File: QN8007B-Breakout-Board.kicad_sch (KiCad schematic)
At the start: 22 parts, among them J1 U.FL, J2 Conn_01x12, U1 QN8007B, Y1 26 MHz

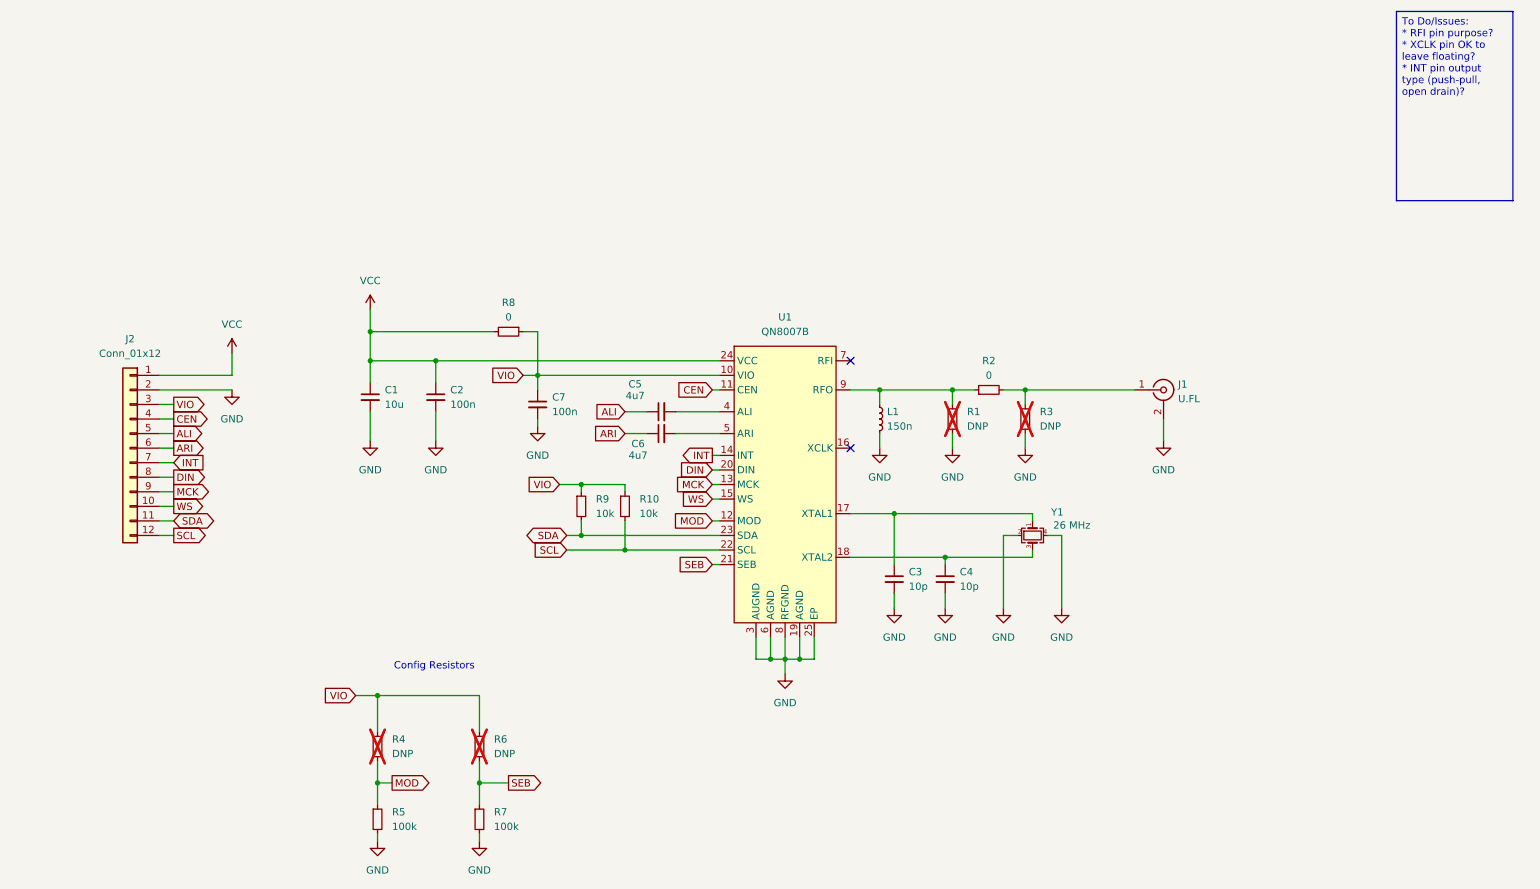
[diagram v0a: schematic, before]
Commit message: Finish routing, small schematic changes to ease routing.
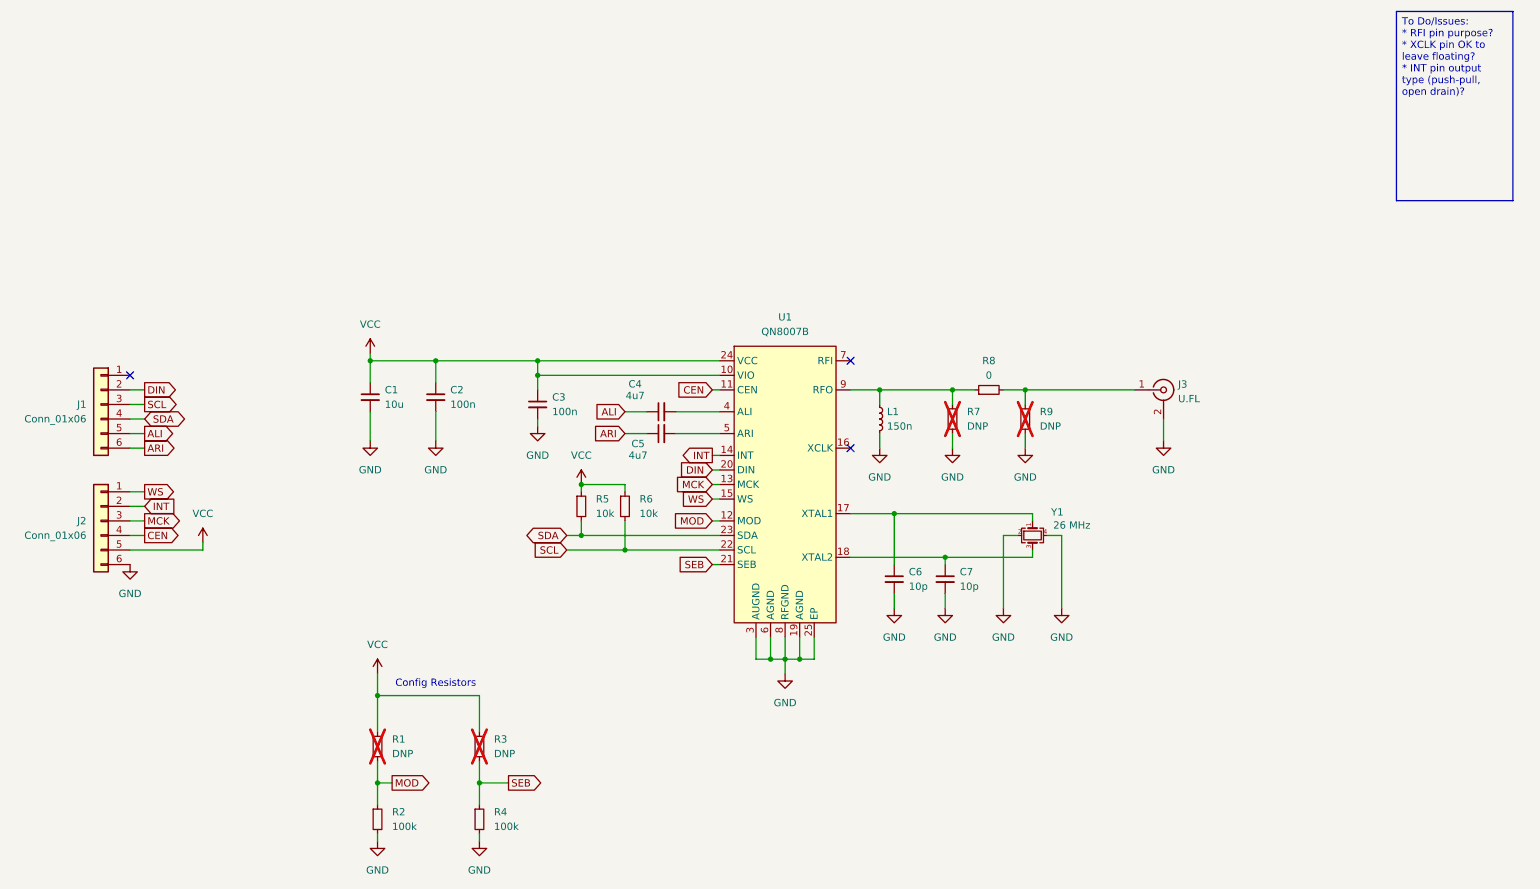
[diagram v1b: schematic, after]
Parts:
- removed J2: Conn_01x12, Connector_PinHeader_2.54mm:PinHeader_1x12_P2.54mm_Vertical, symbol Connector_Generic:Conn_01x12
- removed R8: 0, Resistor_SMD:R_0402_1005Metric, symbol Device:R_Small
- added J1, J2: Conn_01x06, Connector_PinSocket_2.54mm:PinSocket_1x06_P2.54mm_Vertical, symbol Connector_Generic:Conn_01x06
- U1: footprint Package_DFN_QFN:QFN-24-1EP_4x4mm_P0.5mm_EP2.7x2.7mm_ThermalVias -> Package_DFN_QFN:QFN-24-1EP_4x4mm_P0.5mm_EP2.7x2.7mm
- renumbered C7 to C3, C5 to C4, C6 to C5, C3 to C6, C4 to C7, J1 to J3, R4 to R1, R5 to R2, R6 to R3, R7 to R4, R9 to R5, R10 to R6, R1 to R7, R2 to R8, R3 to R9
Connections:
- net VIO is gone; now on net VCC: C3.1, R1.1, R3.1, R5.1, R6.1, U1.10 (VIO)
- net ALI: now also J1.5 (Pin_5)
- net ARI: now also J1.6 (Pin_6)
- net CEN: now also J2.4 (Pin_4)
- net DIN: now also J1.2 (Pin_2)
- net GND: now also J2.6 (Pin_6)
- net INT: now also J2.2 (Pin_2)
- net MCK: now also J2.3 (Pin_3)
- net SCL: now also J1.3 (Pin_3)
- net SDA: now also J1.4 (Pin_4)
- net VCC: now also J2.5 (Pin_5)
- net WS: now also J2.1 (Pin_1)
- no-connect marks 2 -> 3
